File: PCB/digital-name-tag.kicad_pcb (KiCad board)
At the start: 2 copper layers, 39 parts, among them J1 USB_C_Receptacle_USB2.0_14P, J2 Conn_01x20, J3 Conn_01x20, J4 Conn_01x03, Q1 DMG1012T, SW1 SW_Push, U1 RP2040, U2 MCP1700x-120xxMB, U3 W25Q128JVS, Y1 12MHz

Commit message: finnished layout and mostly got routing done
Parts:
- R1, R10, R2, R3, R4, R5, R6, R7, R8, R9: footprint Capacitor_SMD:C_01005_0402Metric -> Resistor_SMD:R_0402_1005Metric
- U3: footprint Package_SO:SOIC-8_5.3x5.3mm_P1.27mm -> easyeda2kicad:USON-8_L3.0-W2.0-P0.50-BL-EP
- moved C7 54.1 mm to (167.8, 89.6), turned to -90 degrees
- moved C8 52.1 mm to (166.8, 89.6), turned to -90 degrees
- moved C9 50.1 mm to (165.8, 89.6), turned to -90 degrees
- moved C12 49.2 mm to (168.4, 84.4)
- moved C11 48.4 mm to (168.4, 81.1)
- moved C18 40.6 mm to (169.0, 64.6)
- moved D1 37.5 mm to (168.0, 74.4), turned to -90 degrees
- moved C17 36.6 mm to (161.6, 73.6), turned to 180 degrees
- moved R8 34.8 mm to (168.6, 63.0), turned to -90 degrees
- moved R9 34.1 mm to (168.4, 66.0), turned to -90 degrees
- moved R2 33.2 mm to (165.0, 62.4)
- moved SW1 32.3 mm to (160.2, 71.2), turned to 180 degrees
- moved R3 29.3 mm to (164.8, 78.2), turned to -90 degrees
- moved R1 28.7 mm to (160.8, 62.3), turned to 180 degrees
- moved R4 28.4 mm to (163.8, 78.2), turned to -90 degrees
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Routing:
- net +3V3: track 0.00 -> 64.3 mm, vias 0 -> 8
- net GPIO0: track 0.00 -> 29.0 mm, vias 0 -> 1
- net GPIO1: track 0.00 -> 27.3 mm, vias 0 -> 1
- net VBUS: track 0.00 -> 24.4 mm
- net GPIO2: track 0.00 -> 23.0 mm, vias 0 -> 1
- net GPIO3: track 0.00 -> 23.0 mm, vias 0 -> 1
- net GPIO28_ADC2: track 0.00 -> 22.4 mm, vias 0 -> 4
- net GPIO15: track 0.00 -> 21.7 mm, vias 0 -> 1
- net GPIO29_ADC3: track 0.00 -> 21.1 mm, vias 0 -> 2
- net D-: track 0.00 -> 20.9 mm
- net SWCLK: track 0.00 -> 20.0 mm, vias 0 -> 1
- net D+: track 0.00 -> 19.9 mm
- net GPIO16: track 0.00 -> 19.5 mm, vias 0 -> 2
- net GPIO4: track 0.00 -> 18.4 mm
- net GPIO5: track 0.00 -> 18.3 mm, vias 0 -> 1
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- added copper zone on B.Cu, net GND
- added copper zone on F.Cu, net GND
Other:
- board outline added: 21 x 51 mm

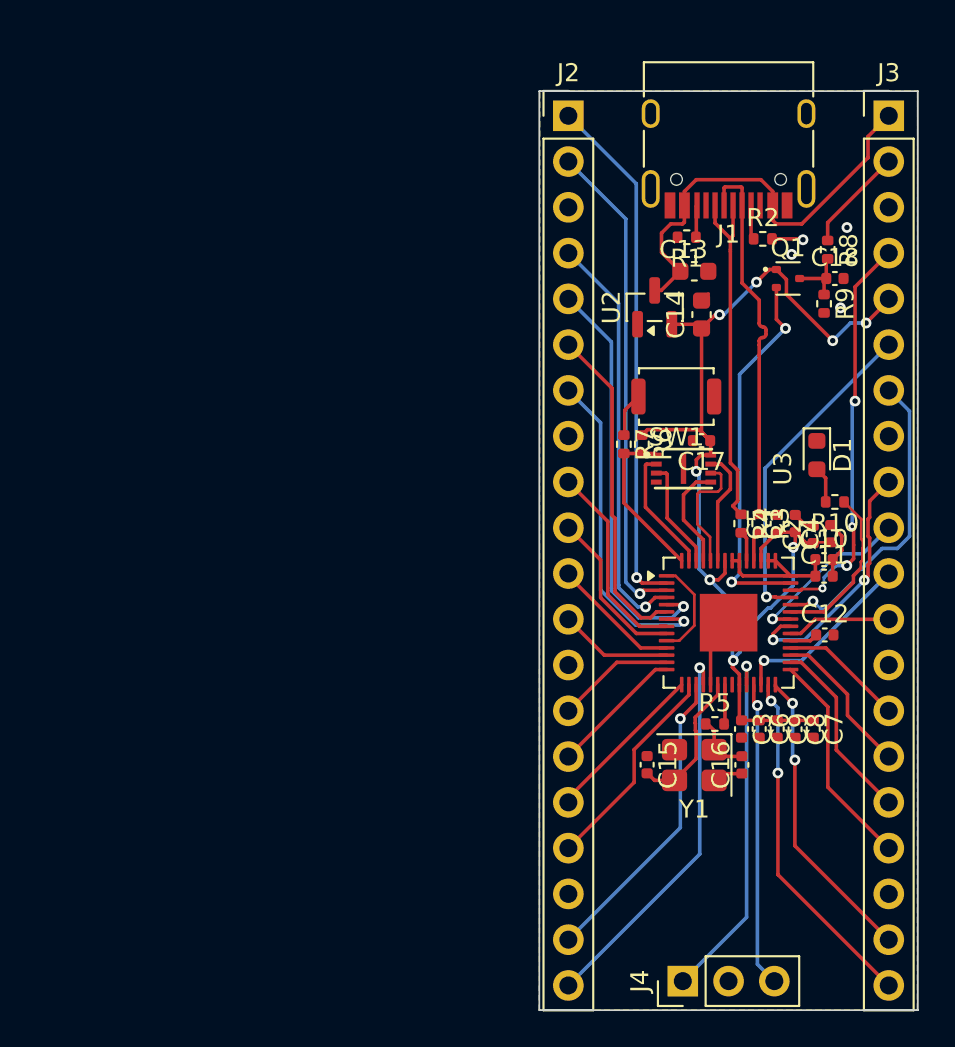
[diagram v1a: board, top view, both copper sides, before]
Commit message: fixed DRC errors
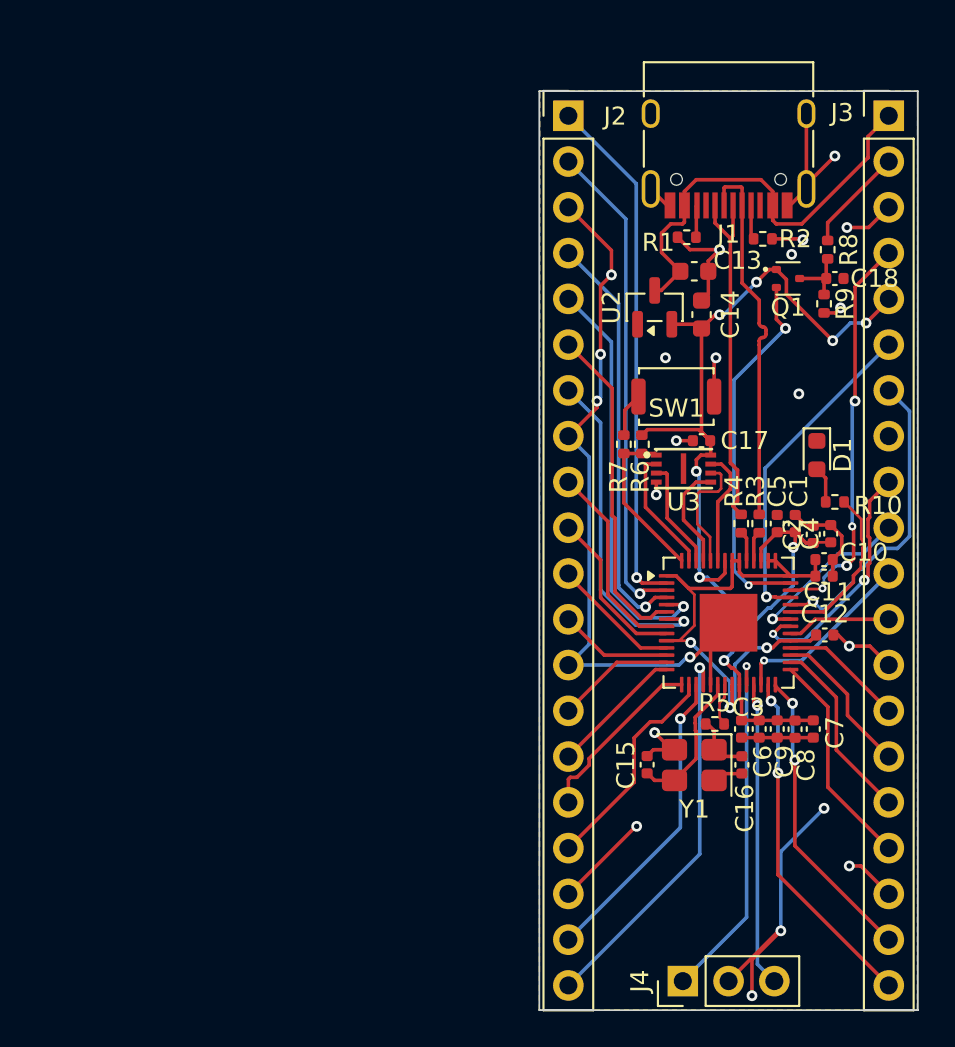
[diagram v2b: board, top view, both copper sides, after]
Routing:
- net GND: track 12.5 -> 109.3 mm, vias 4 -> 22
- net +1V1: track 15.1 -> 33.9 mm, vias 0 -> 3
- net +3V3: track 64.3 -> 65.3 mm
- net GPIO12: track 9.14 -> 9.96 mm

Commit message: fixed BOM and got the pcb added to cart I think i forgot to save the BOM last time but i ended up changing a good portion of it anyways to change from exstended pcba to basic.
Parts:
- U3: value W25Q128JVS -> IS25WP016D-JULE-TR
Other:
- board text added: "REV A 2026"

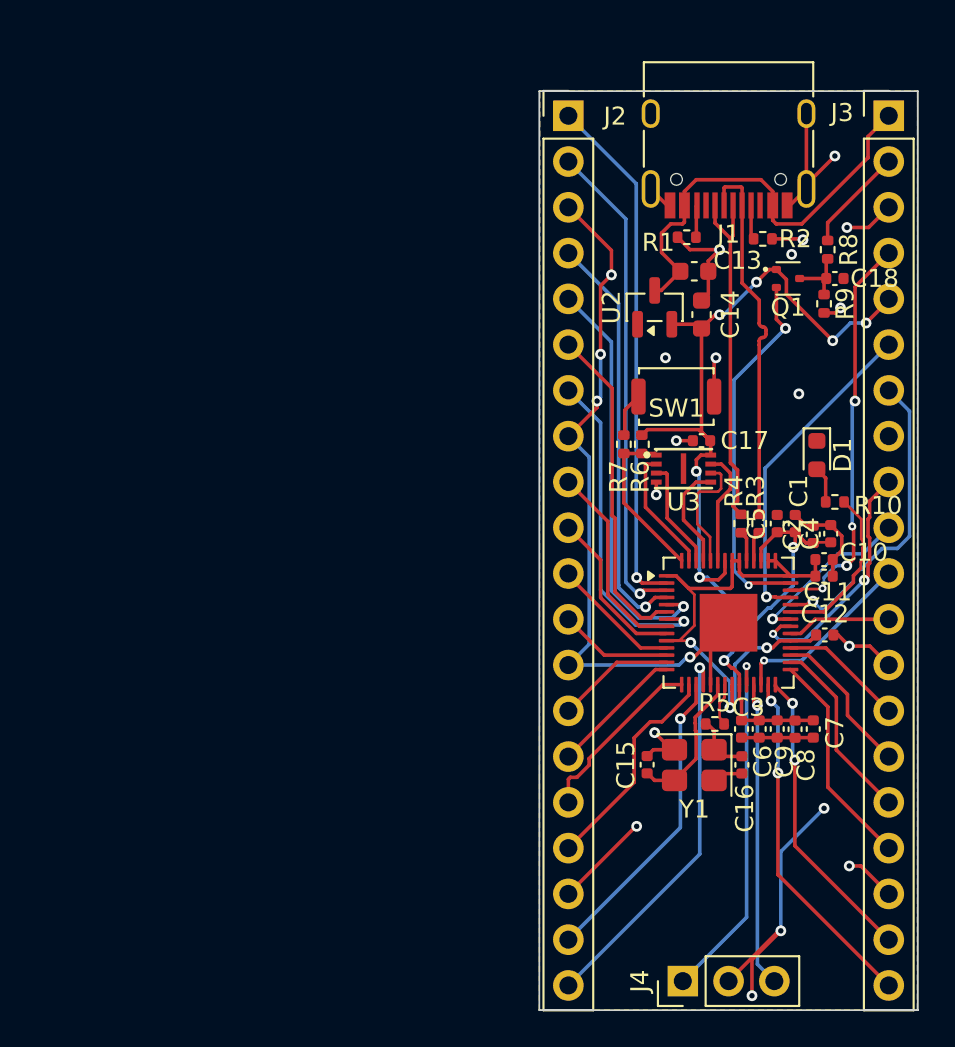
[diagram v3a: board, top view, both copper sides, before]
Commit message: fileted the corners.
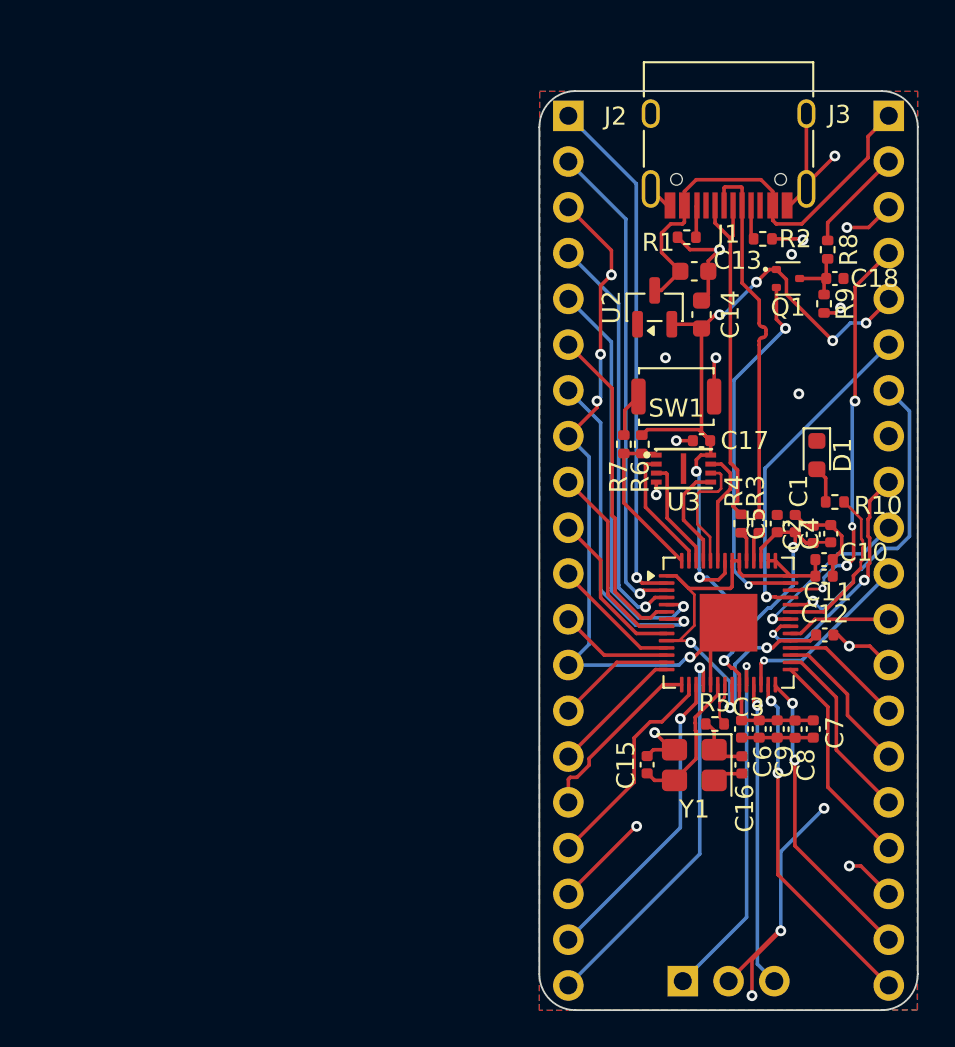
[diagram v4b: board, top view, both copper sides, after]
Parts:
- J2, J3, J4: moved to B.Cu
- turned J2 to 180 degrees
- turned J3 to 180 degrees
- turned J4 to -90 degrees
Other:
- outline, holes or cut-outs redrawn

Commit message: added silkscreen art
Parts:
- added G***: LOGO, LOGO, F.Cu at (158.9, 98.8)
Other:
- board text added: "<- press for stuff"
- board text added: "Magic smoke"
- board text added: "Now with 100% more electrons"
- board text added: "if you are reading this then you are holding the board wrong."

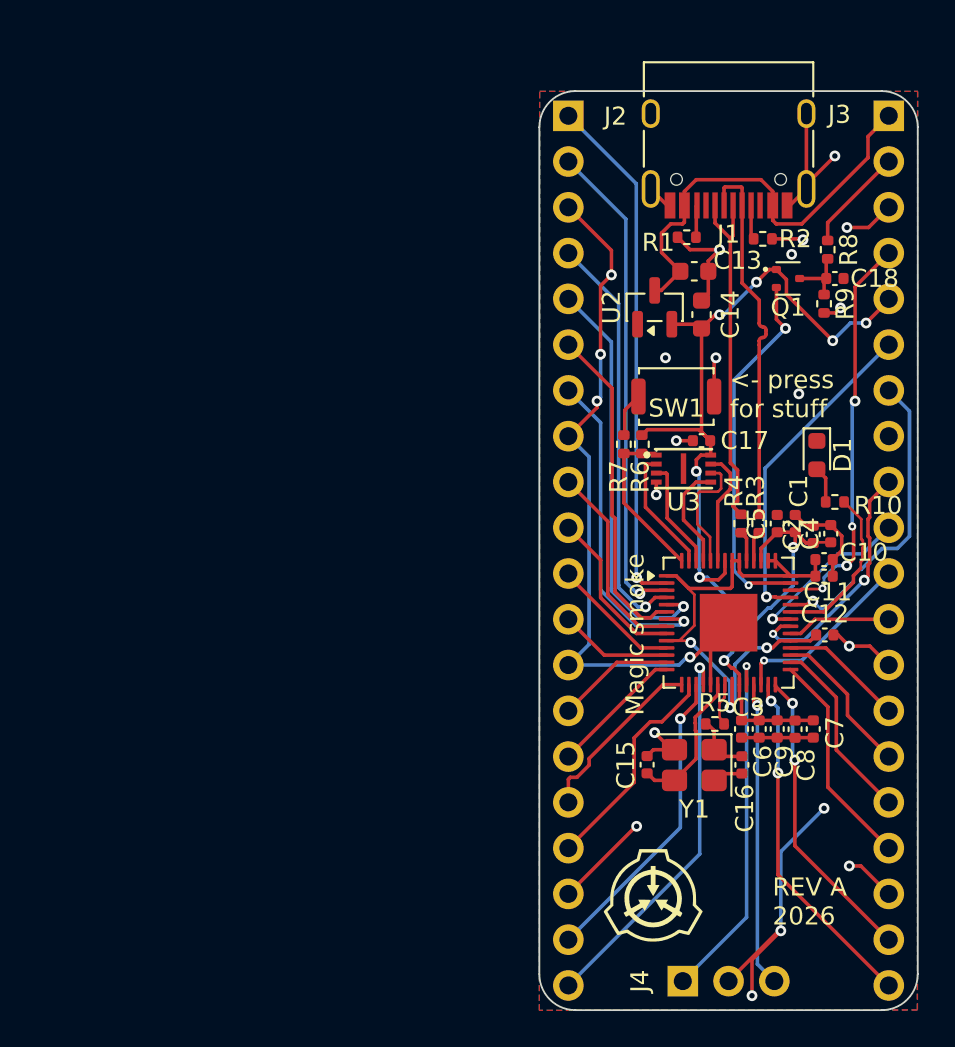
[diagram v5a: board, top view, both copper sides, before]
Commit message: updated the schematic and pcb to have the correct power rails.
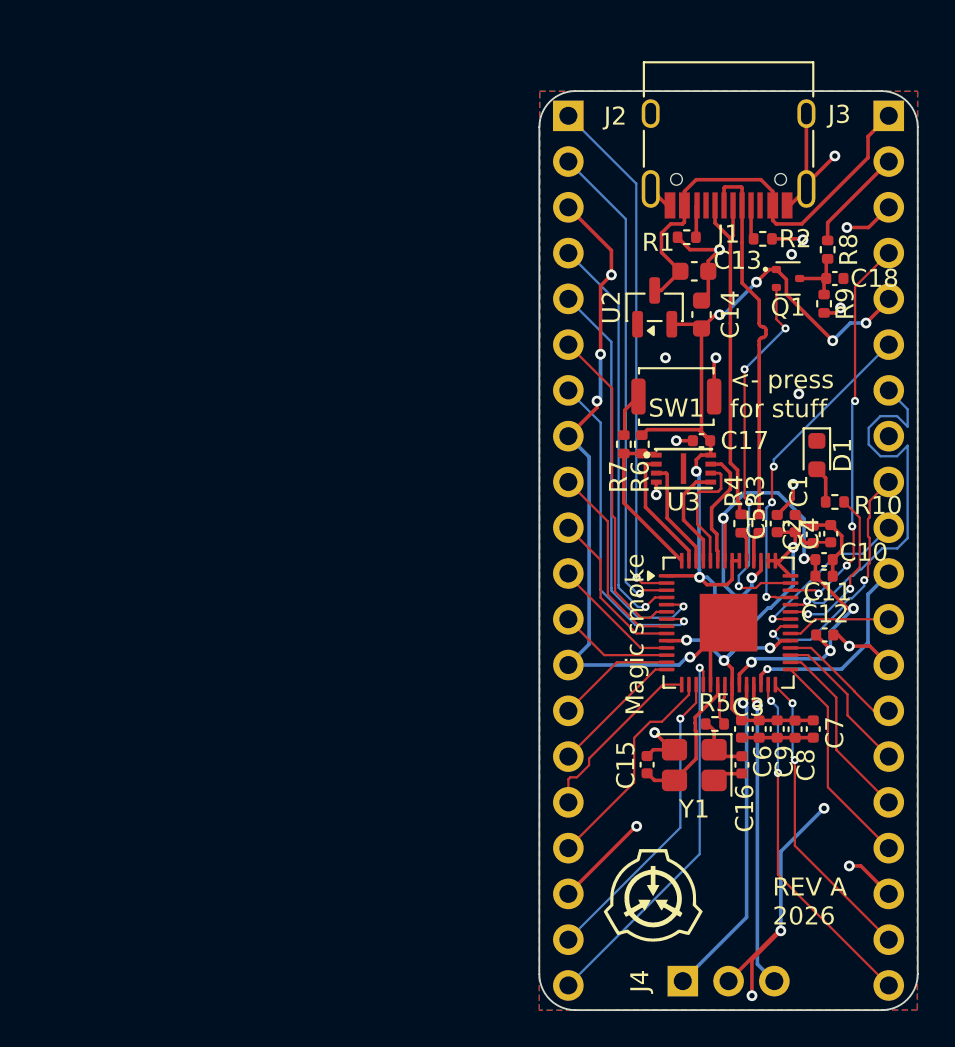
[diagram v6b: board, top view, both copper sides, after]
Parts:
- D1: value LED -> Green
- U3: value IS25WP016D-JULE-TR -> W25Q128JVS
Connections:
- U1 pad 1: +1V1 -> +3V3
- U1 pad 10: +1V1 -> +3V3
- U1 pad 22: +1V1 -> +3V3
- U1 pad 23: +3V3 -> +1V1
- U1 pad 33: +1V1 -> +3V3
- U1 pad 42: +1V1 -> +3V3
- U1 pad 43: +1V1 -> +3V3
- U1 pad 44: +1V1 -> +3V3
- U1 pad 45: +3V3 -> +1V1
- U1 pad 48: +1V1 -> +3V3
- U1 pad 49: +1V1 -> +3V3
- U1 pad 50: +3V3 -> +1V1
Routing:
- net +3V3: track 65.3 -> 77.3 mm, vias 8 -> 10
- net GPIO26_ADC0: track 17.3 -> 22.0 mm
- net GND: track 109.3 -> 111.4 mm, vias 22 -> 23
- net SWCLK: track 20.0 -> 18.1 mm
- net +1V1: track 33.9 -> 32.5 mm, vias 3 -> 6
- net RUN: track 10.3 -> 11.5 mm
- net GPIO29_ADC3: track 20.6 -> 21.1 mm, vias 2 -> 4
- net GPIO25: track 9.28 -> 9.35 mm, vias 0 -> 2
- net GPIO27_ADC1: track 18.2 -> 18.3 mm, vias 1 -> 3
